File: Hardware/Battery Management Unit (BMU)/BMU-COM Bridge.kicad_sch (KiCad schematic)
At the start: 35 parts, among them T1 CEP99-102, T2 CEP99-102, U3 PESD5V0L2BT, U4 BQ79600PWRQ1, U5 PESD5V0L2BT

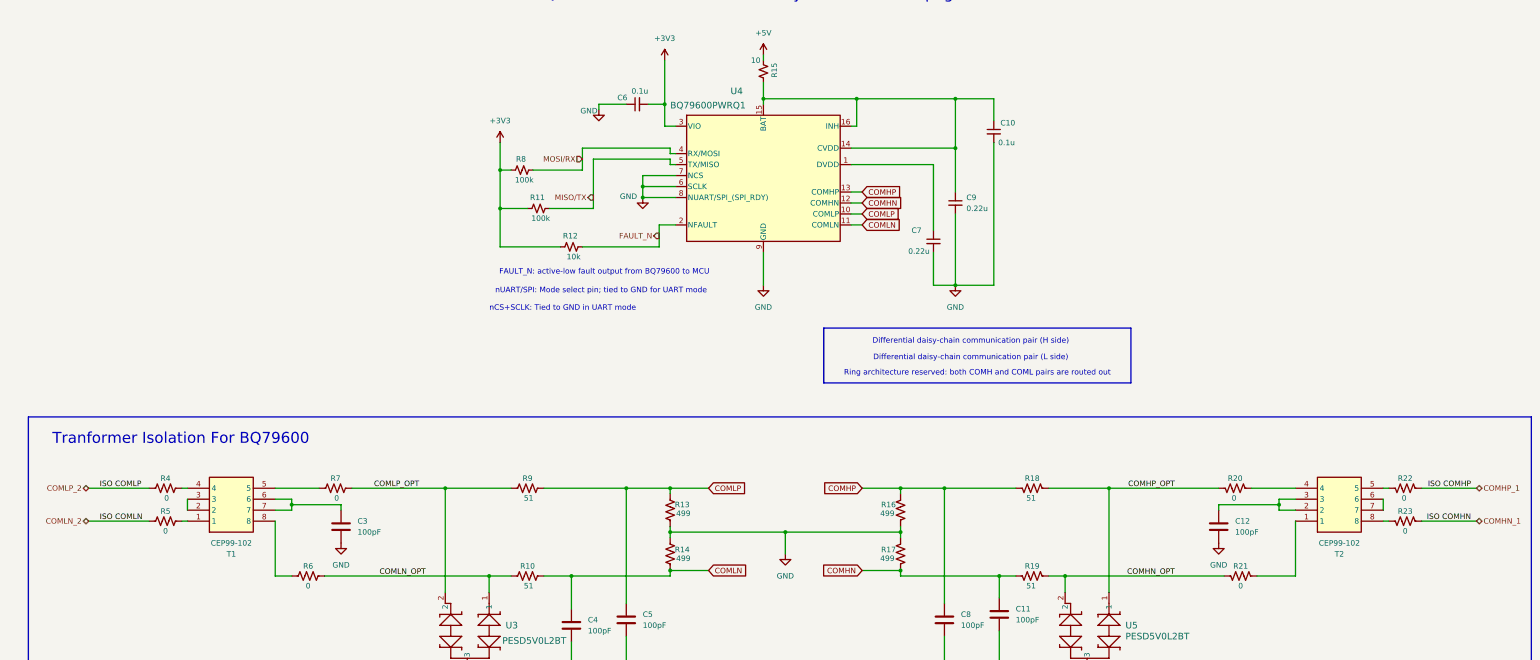
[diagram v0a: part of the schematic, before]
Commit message: Schematic polish -- fixed to best standards, cleaned up for ERCs, etc
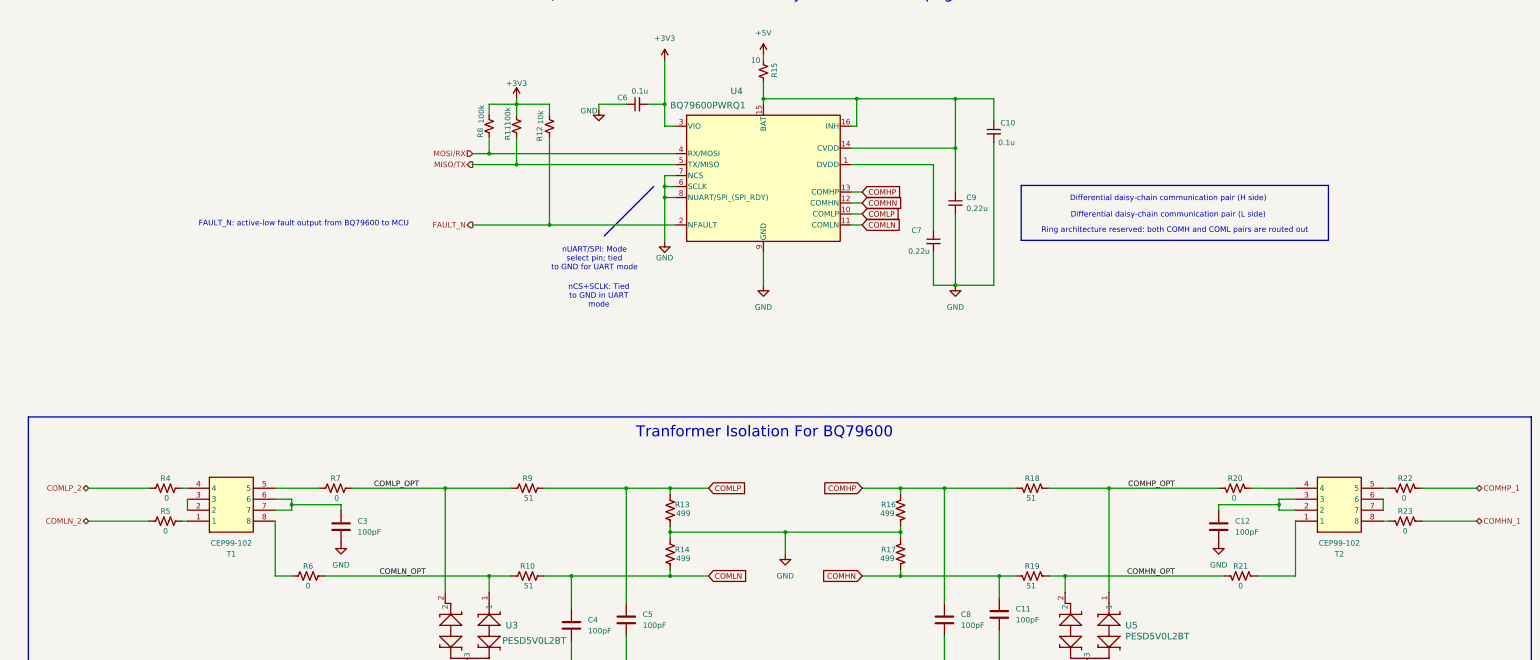
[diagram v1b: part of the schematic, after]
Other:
- moved on the sheet: R11, R12, R8

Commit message: update libraries+bmu
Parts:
- T1, T2: footprint CEP99-102:CEP99102 -> Footprints:CEP99102
- U3, U5: footprint PESD5V0L2BT:SOT23_NEX -> Footprints:SOT23_NEX
- U4: footprint BQ79600:TSSOP16_PW_TEX -> Footprints:TSSOP16_PW_TEX
- renumbered R9 to R10, R10 to R11, R11 to R9
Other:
- moved on the sheet: C10, C11, C12, C3, C4, C5, C6, C7, C8, C9, R10, R11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

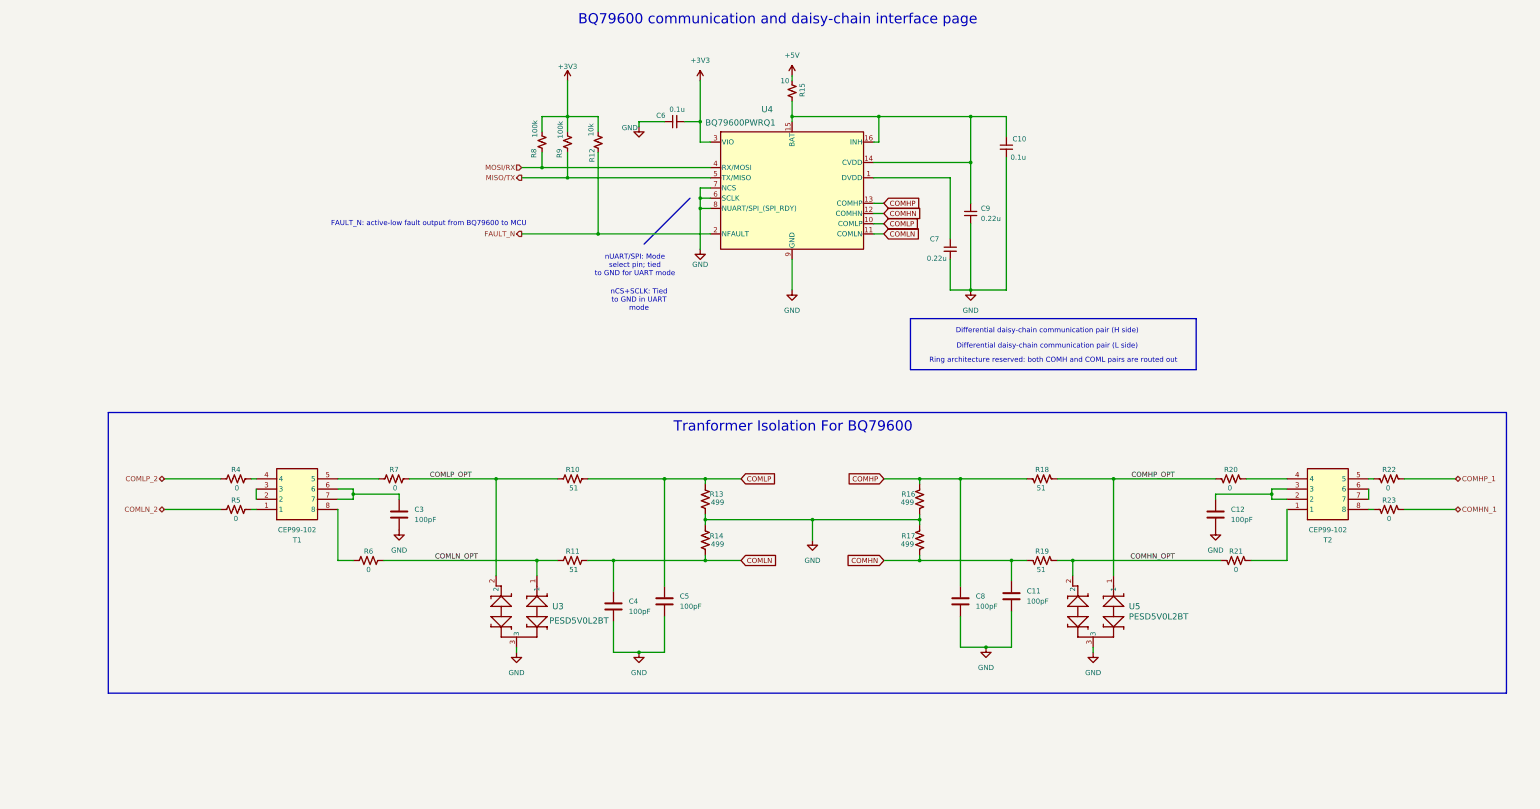
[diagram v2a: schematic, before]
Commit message: Schematic cleanup; lots of missing library files
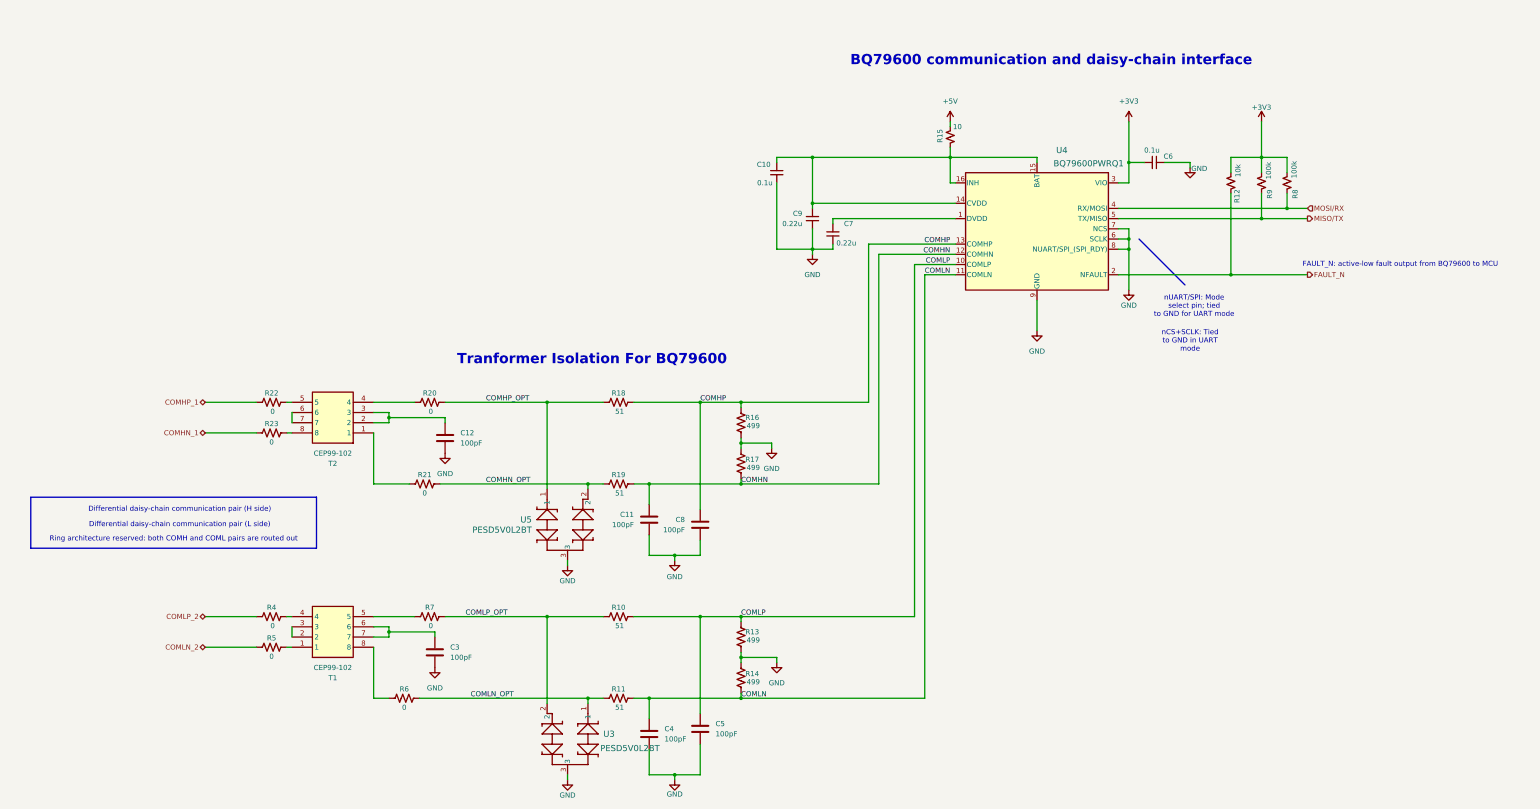
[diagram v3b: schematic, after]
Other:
- note added: "BQ79600 communication and daisy-chain interface"
- note removed: "BQ79600 communication and daisy-chain interface page"
- moved on the sheet: C10, C11, C12, C3, C4, C5, C6, C7, C8, C9, R10, R11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

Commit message: doubled up pin for bmu
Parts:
- renumbered C9 to C10, C7 to C11, C6 to C12, C12 to C4, C11 to C5, C4 to C6, C8 to C7, C5 to C8, C10 to C9, R20 to R10, R7 to R11, R18 to R12, R19 to R13, R10 to R14, R11 to R15, R13 to R18, R14 to R19, R15 to R20, R12 to R21, R9 to R22, R8 to R23, R22 to R4, R23 to R5, R4 to R6, R5 to R7, R6 to R8, R21 to R9, U5 to U3, U3 to U4, U4 to U5
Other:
- moved on the sheet: C10, C11, C12, C3, C4, C5, C6, C7, C8, C9, R10, R11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

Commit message: finish! update bmu layout+BOM
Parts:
- removed T1, T2: CEP99-102, Footprints:CEP99102, symbol CEP99-102:CEP99-102
- added T1, T2: HM2147NLT, Footprints:HM2147NLT, symbol HM2147NLT:HM2147NLT
- C10, C11: DIS (none) -> DigiKey; DPN (none) -> 311-1887-1-ND; MFR (none) -> YAGEO; MPN (none) -> CC0805KKX7R9BB224; Purchase Link (none) -> https://www.digikey.com/en/products/detail/yageo/CC0805KKX7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
- C12, C9: value 0.1u -> 100n; DIS (none) -> DigiKey; DPN (none) -> 311-1140-1-ND; MFR (none) -> YAGEO; MPN (none) -> CC0805KRX7R9BB104; Purchase Link (none) -> https://www.digikey.com/en/products/detail/yageo/CC0805KRX7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
- C3, C4, C5, C6, C7, C8: DIS (none) -> DigiKey; DPN (none) -> 311-4295-1-ND; MFR (none) -> YAGEO; MPN (none) -> CC0805KRNPO9BN101; Purchase Link (none) -> https://www.digikey.com/en/products/detail/yageo/CC0805KRNP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
- R10, R11, R4, R5, R6, R7, R8, R9: DIS (none) -> DigiKey; DPN (none) -> 311-0.0ARCT-ND; MFR (none) -> YAGEO; MPN (none) -> RC0805JR-070RL; Purchase Link (none) -> https://www.digikey.com/en/products/detail/yageo/RC0805JR-0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
- R12, R13, R14, R15: DIS (none) -> DigiKey; DPN (none) -> 311-51.0CRCT-ND; MFR (none) -> YAGEO; MPN (none) -> RC0805FR-0751RL; Purchase Link (none) -> https://www.digikey.com/en/products/detail/yageo/RC0805FR-0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
- R16, R17, R18, R19: DIS (none) -> DigiKey; DPN (none) -> 311-499CRCT-ND; MFR (none) -> YAGEO; MPN (none) -> RC0805FR-07499RL; Purchase Link (none) -> https://www.digikey.com/en/products/detail/yageo/RC0805FR-0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
- R20: DIS (none) -> DigiKey; DPN (none) -> 311-10.0CRCT-ND; MFR (none) -> YAGEO; MPN (none) -> RC0805FR-0710RL; Purchase Link (none) -> https://www.digikey.com/en/products/detail/yageo/RC0805FR-0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
- R21: DIS (none) -> DigiKey; DPN (none) -> 311-10.0KCRCT-ND; MFR (none) -> YAGEO; MPN (none) -> RC0805FR-0710KL; Purchase Link (none) -> https://www.digikey.com/en/products/detail/yageo/RC0805FR-0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
- R22, R23: DIS (none) -> DigiKey; DPN (none) -> 311-100KCRCT-ND; MFR (none) -> YAGEO; MPN (none) -> RC0805FR-07100KL; Purchase Link (none) -> https://www.digikey.com/en/products/detail/yageo/RC0805FR-0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
- U3, U4: DIS (none) -> DigiKey; DPN (none) -> 1727-3834-1-ND; MFR (none) -> Nexperia USA Inc.; MPN (none) -> PESD5V0L2BT,215; Purchase Link (none) -> https://www.digikey.com/en/products/detail/nexperia-usa-inc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
- U5: DIS (none) -> DigiKey; DPN (none) -> 296-BQ79600PWRQ1CT-ND; MFR (none) -> Texas Instruments; MPN (none) -> BQ79600PWRQ1; Purchase Link (none) -> https://www.digikey.com/en/products/detail/texas-instrument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
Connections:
- net at R9.1: now also T1.4 (SEC_1)
- net at R4.2: now also T1.1 (PRI_1)
- net at R5.2: now also T1.3 (PRI_3)
- net at R8.1: now also T2.4 (SEC_1)
- net at R10.1: now also T1.6 (SEC_3)
- net at C4.1: now also T1.5 (SEC_2)
- net at R7.2: now also T2.3 (PRI_3)
- net at R6.2: now also T2.1 (PRI_1)
- net at R11.1: now also T2.6 (SEC_3)
- net at C3.1: now also T2.5 (SEC_2)
- no-connect marks 0 -> 2
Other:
- note added: "Transformer Isolation For BQ79600"
- note removed: "Tranformer Isolation For BQ79600"
- moved on the sheet: R4, R5, R6, R7
